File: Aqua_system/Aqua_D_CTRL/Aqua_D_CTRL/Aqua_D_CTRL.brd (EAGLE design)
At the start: 150 x 120 mm, 233 parts, among them IC1 SN65HVD3082EDR, IC2 CSTNE8M00G520000R0, IC3 LT6106CS5#TRPBF, IC4 LT6106CS5#TRPBF, IC5 TPS54202DDCR, IC6 LD1117S33TR, IC8 LM317AEMP, J1 ESP32-PICO-KIT, K1 KB20C06A, K2 KB20C06A, Q1 DMP6185SEQ-13, Q10 BC817, Q11 2N7002, Q12 DMP6185SEQ-13, Q13 2N7002, Q14 DMP6185SEQ-13, Q15 2N7002, Q16 DMP6185SEQ-13, Q17 BC817, Q18 BC817, Q19 BC817, Q2 2N7002, Q20 BC817, Q21 BC817, Q22 BC817, Q23 BC817, Q3 DMP6185SEQ-13, Q4 2N7002, Q5 DMP6185SEQ-13, Q6 DMP6185SEQ-13, Q7 2N7002, Q8 DMP6185SEQ-13, Q9 2N7002, SW1 L101011MS02Q, U1 S7G2LQFP176, X1 B2B-XH-AM(LF)(SN), X10 726386-2TE_726386-2, X11 282834-2, X12 RJ45-8L-B, X13 MICROMATCH-16, X14 RJ45-8L-B, X2 WF2549-2WS05S0B01, X3 282834-3, X4 282834-3, X5 726386-2TE_726386-2, X6 726386-2TE_726386-2, X7 726386-2TE_726386-2, X8 726386-2TE_726386-2, X9 726386-2TE_726386-2

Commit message: HW00.00 update
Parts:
- added C40: 1uF/25V, Labops_Lib_AH:0603
- added C41: 100nF/50V, Labops_Lib_AH:0603
- added R84: 10K 1%, Labops_Lib_AH:R0603
- moved C59 7.49 mm to (71.5, 49.1)
- moved C44 3.81 mm to (81.0, 72.1)
- moved C55 3.81 mm to (83.1, 72.1)
- moved C56 2.79 mm to (71.4, 55.9)
- moved X2 2.54 mm to (64.9, 73.3)
- moved C57 0.89 mm to (71.4, 53.7)
- moved D9 0.18 mm to (63.9, 23.7), turned to 180 degrees
- moved D5 0.13 mm to (67.3, 23.7), turned to 180 degrees
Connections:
- removed net MCU_RESET: U1.67
- removed net N$87: C58.2, U1.97
- new net NRST: C41.1, R84.2, U1.67, X2.10
- net GND: now also C40.2, C41.2, X2.3, X2.5, X2.9
- net VCC: now also C40.1, C58.2, R84.1, U1.97, X2.1
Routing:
- net VCC: track 320.1 -> 391.5 mm, vias 6 -> 16
- net DO_PH_SENSOR_ON: track 0.00 -> 38.0 mm, vias 0 -> 2
- net NRST: track 0.00 -> 34.2 mm, vias 0 -> 1
- net GND: track 35.5 -> 44.4 mm
- net AI_I_SENSE_PH_SENSOR: track 41.3 -> 36.3 mm
- net N$87: track 3.91 -> 0.00 mm
- net DBG_SWO: track 14.3 -> 16.7 mm
- net DBG_SWCLK: track 13.0 -> 15.1 mm
- net AI_I_SENSE_CONDUTIV_SENSOR: track 25.1 -> 26.4 mm
- net DBG_SWDIO: track 12.4 -> 13.5 mm

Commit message: HW00.00 Layout Ongoing
Ongoing Changes On Layout
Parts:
- removed C54: 100nF/50V, Labops_Lib_AH:0603
- removed R98, R99: 10K 1%, Labops_Lib_AH:R0603
- removed U1: S7G2LQFP176, 3D_MIG_Controller:LQFP176_24X24
- added U2: RENESAS_R7FA6M5BG3CFBLQFP_144_20X20_REN-M, 3D_MIG_Controller:LQFP_144_20X20_REN-M
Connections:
- removed net N$40: U1.29
- removed net N$58: IC2.1, R93.2, U1.24
- removed net N$60: U1.30
- removed net N$72: C54.2, U1.62
- removed net N$85: R98.2, U1.64
- removed net N$86: R99.2, U1.65
- removed net N$93: U1.160
- new net AVCC0: U2.127
- new net AVSS0: U2.128
- new net N$66: IC2.1, R93.2, U2.20
- new net VBATT: U2.14
- new net VCC_2: U2.81
- new net VCC_3: U2.90
- new net VCC_4: U2.99
- new net VCC_5: U2.111
- new net VCC_6: U2.121
- new net VCC_USBHS: U2.40
- new net VCL: U2.92
- new net VREFH: U2.126
- new net VREFH0: U2.130
- new net VREFL: U2.125
- new net VREFL0: U2.129
- new net VSS: U2.141
- new net VSS_2: U2.82
- new net VSS_3: U2.91
- new net VSS_4: U2.100
- new net VSS_5: U2.112
- new net VSS_6: U2.122
- new net VSS_USB: U2.37
- net /DO_COMM_RX_EN: now also U2.32; no longer U1.40
- net AI_24V0: no longer U1.144
- net AI_I_SENSE_CONDUTIV_SENSOR: no longer U1.146
- net AI_I_SENSE_PH_SENSOR: no longer U1.140
- net AI_V_PH_SENSOR: no longer U1.142
- net DBG_SWCLK: now also U2.72; no longer U1.88
- net DBG_SWDIO: now also U2.73; no longer U1.89
- net DBG_SWO: now also U2.74; no longer U1.90
- net DI_DOSING_EN: now also U2.31; no longer U1.39
- net DI_UART_RX_ESP32: now also U2.71; no longer U1.87
- net DI_USART_RX: now also U2.35; no longer U1.43
- net DO_7XSEGMENT_1_EN: now also U2.1; no longer U1.1
- net DO_7XSEGMENT_2_EN: now also U2.2; no longer U1.2
- net DO_7XSEGMENT_3_EN: now also U2.3; no longer U1.3
- net DO_BCD_A: no longer U1.130
- net DO_BCD_B: no longer U1.129
- net DO_BCD_C: no longer U1.128
- net DO_BCD_D: no longer U1.127
- net DO_COMM_TX_EN: now also U2.33; no longer U1.41
- net DO_CONDUCTIV_PUMP_ON_LED: now also U2.8; no longer U1.8
- net DO_CONDUCTIV_SENSOR_DISPLAY_ON: now also U2.7; no longer U1.7
- net DO_CONDUCTIV_SENSOR_ON: no longer U1.132
- net DO_CTRL_GREEN_STATUS_LED: now also U2.5; no longer U1.5
- net DO_CTRL_RED_STATUS_LED: now also U2.6; no longer U1.6
- net DO_CTRL_YELLOW_STATUS_LED: now also U2.4; no longer U1.4
- net DO_ESP32_EN: now also U2.69; no longer U1.85
- net DO_PH_PUMP_ON_LED: now also U2.10; no longer U1.10
- net DO_PH_SENSOR_DISPLAY_ON: now also U2.9; no longer U1.9
- net DO_PH_SENSOR_ON: no longer U1.131
- net DO_UART_TX_ESP32: now also U2.70; no longer U1.86
- net DO_USART_TX: now also U2.34; no longer U1.42
- net DO_V_CONDUCTIV_PUMP_ON: no longer U1.91
- net DO_V_PH_PUMP_ON: no longer U1.92
- net GND: now also U2.18, U2.48, U2.67; no longer C54.1, R98.1, R99.1, U1.111, U1.124, U1.139, U1.150, U1.156, U1.157, U1.170, U1.22, U1.28, U1.35, U1.45, U1.60, U1.63, U1.66, U1.83, U1.98
- net N$55: now also U2.19; no longer U1.23
- net N$59: no longer U1.27
- net N$63: now also U2.15; no longer U1.19
- net N$88: no longer U1.112
- net N$90: no longer U1.148
- net NRST: now also U2.55; no longer U1.67
- net VCC: now also U2.142, U2.21, U2.49, U2.68; no longer U1.110, U1.123, U1.138, U1.149, U1.155, U1.158, U1.171, U1.25, U1.61, U1.84, U1.97
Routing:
- net VCC: track 391.5 -> 368.8 mm
- net DO_7XSEGMENT_1_EN: track 19.8 -> 2.12 mm
- net DO_V_CONDUCTIV_PUMP_ON: track 32.1 -> 20.9 mm
- net DO_V_PH_PUMP_ON: track 14.1 -> 3.30 mm
- net N$58: track 8.07 -> 0.00 mm
- net DBG_SWCLK: track 15.1 -> 9.12 mm
- net DO_COMM_TX_EN: track 5.33 -> 0.21 mm
- net N$72: track 4.86 -> 0.00 mm
- net N$66: track 0.00 -> 4.65 mm
- net N$85: track 4.43 -> 0.00 mm
- net N$86: track 4.21 -> 0.00 mm
- net DBG_SWO: track 16.7 -> 12.5 mm
- net DO_UART_TX_ESP32: track 4.04 -> 0.14 mm
- net DO_USART_TX: track 5.97 -> 2.38 mm
- net DBG_SWDIO: track 13.5 -> 10.4 mm
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
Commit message: HW00.00 ongoing
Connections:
- removed net VCC_2: U2.81
- removed net VCC_3: U2.90
- removed net VCC_4: U2.99
- removed net VCL: U2.92
- removed net VSS_2: U2.82
- removed net VSS_3: U2.91
- removed net VSS_4: U2.100
- net DO_BCD_A: now also U2.106
- net DO_BCD_B: now also U2.105
- net DO_BCD_C: now also U2.104
- net DO_BCD_D: now also U2.103
- net DO_CONDUCTIV_SENSOR_ON: now also U2.108
- net DO_PH_SENSOR_ON: now also U2.107
- net DO_V_CONDUCTIV_PUMP_ON: now also U2.75
- net DO_V_PH_PUMP_ON: now also U2.76
- net GND: now also U2.100, U2.82, U2.91
- net N$88: now also U2.92
- net VCC: now also U2.81, U2.90, U2.99
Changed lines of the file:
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@@
 <contactref element="U2" pad="48"/>
 <contactref element="U2" pad="67"/>
+<contactref element="U2" pad="82"/>
+<contactref element="U2" pad="91"/>
+<contactref element="U2" pad="100"/>
 <wire x1="130.214" y1="99.822" x2="131.358" y2="117.094" width="0" layer="19" extent="1-1"/>
 <wire x1="125.818" y1="99.822" x2="128.866" y2="99.822" width="0" layer="19" extent="1-1"/>
@@
 <wire x1="48.094" y1="80.01" x2="50.275" y2="77.216" width="0" layer="19" extent="1-1"/>
 <wire x1="80.518" y1="64.69575" x2="81.026" y2="72.986" width="0" layer="19" extent="1-1"/>
+<wire x1="76.02025" y1="58.166" x2="80.518" y2="64.69575" width="0" layer="19" extent="1-1"/>
+<wire x1="76.02025" y1="53.594" x2="76.02025" y2="58.166" width="0" layer="19" extent="1-1"/>
+<wire x1="76.02025" y1="49.022" x2="76.02025" y2="53.594" width="0" layer="19" extent="1-1"/>
+<wire x1="70.651" y1="49.149" x2="76.02025" y2="49.022" width="0" layer="19" extent="1-1"/>
+<wire x1="70.524" y1="60.96" x2="70.524" y2="55.88" width="0" layer="19" extent="1-1"/>
 <wire x1="90.17" y1="64.69575" x2="86.995" y2="72.986" width="0" layer="19" extent="1-1"/>
+<wire x1="72.048" y1="40.386" x2="70.651" y2="49.149" width="0" layer="19" extent="1-1"/>
 <wire x1="70.612" y1="92.749" x2="79.604" y2="96.266" width="0" layer="19" extent="1-1"/>
 <wire x1="68.58" y1="92.749" x2="70.612" y2="92.749" width="0" layer="19" extent="1-1"/>
 <wire x1="62.738" y1="94.742" x2="68.58" y2="92.749" width="0" layer="19" extent="1-1"/>
 <wire x1="60.198" y1="90.082" x2="62.738" y2="94.742" width="0" layer="19" extent="1-1"/>
-<wire x1="70.524" y1="60.96" x2="60.198" y2="62.904" width="0" layer="19" extent="1-1"/>
-<wire x1="70.524" y1="55.88" x2="70.524" y2="60.96" width="0" layer="19" extent="1-1"/>
-<wire x1="72.048" y1="40.386" x2="70.651" y2="49.149" width="0" layer="19" extent="1-1"/>
 <wire x1="59.563" y1="44.87" x2="70.651" y2="49.149" width="0" layer="19" extent="1-1"/>
 <wire x1="55.819" y1="46.566" x2="59.563" y2="44.87" width="0" layer="19" extent="1-1"/>
@@
 <contactref element="U2" pad="21"/>
 <contactref element="U2" pad="49"/>
+<contactref element="U2" pad="81"/>
+<contactref element="U2" pad="90"/>
+<contactref element="U2" pad="99"/>
 <wire x1="115.316" y1="74.002" x2="113.284" y2="74.002" width="0" layer="19" extent="1-1"/>
 <wire x1="97.71575" y1="55.118" x2="102.088" y2="55.86" width="0" layer="19" extent="1-1"/>
@@
 <wire x1="84.836" y1="69.596" x2="91.396" y2="69.044" width="0" layer="19" extent="1-1"/>
 <wire x1="95.758" y1="38.442" x2="95.758" y2="38.481" width="0" layer="19" extent="1-1"/>
+<wire x1="76.02025" y1="54.102" x2="73.244" y2="54.86" width="0" layer="19" extent="1-1"/>
+<wire x1="76.02025" y1="49.53" x2="73.14" y2="48.36" width="0" layer="19" extent="1-1"/>
+<wire x1="76.02025" y1="58.674" x2="74.187" y2="61.36" width="0" layer="19" extent="1-1"/>
 <wire x1="80.01" y1="64.69575" x2="79.896" y2="68.847" width="0" layer="19" extent="1-1"/>
 <wire x1="66.36" y1="24.749" x2="66.548" y2="28.956" width="0" layer="19" extent="1-1"/>
@@
 <wire x1="64.174" y1="62.904" x2="62.23" y2="62.904" width="0.254" layer="1"/>
 <wire x1="65.13" y1="63.86" x2="64.174" y2="62.904" width="0.254" layer="1"/>
+<contactref element="U2" pad="76"/>
+<wire x1="65.13" y1="63.86" x2="76.02025" y2="61.214" width="0" layer="19" extent="1-1"/>
 </signal>
 <signal name="V_PH" class="3">
@@
 <wire x1="77.089" y1="42.164" x2="77.089" y2="44.069" width="0.2032" layer="1"/>
 <wire x1="77.089" y1="44.069" x2="76.798" y2="44.36" width="0.2032" layer="1"/>
+<contactref element="U2" pad="107"/>
+<wire x1="76.798" y1="44.36" x2="76.02025" y2="45.466" width="0" layer="19" extent="1-1"/>
 </signal>
 <signal name="AI_I_SENSE_PH_SENSOR" class="3">
@@
 <wire x1="64.389" y1="47.664" x2="61.595" y2="44.87" width="0.254" layer="1"/>
 <wire x1="64.389" y1="61.976" x2="64.389" y2="47.664" width="0.254" layer="1"/>
+<contactref element="U2" pad="75"/>
+<wire x1="64.741" y1="64.36" x2="76.02025" y2="61.722" width="0" layer="19" extent="1-1"/>
 </signal>
 <signal name="V_CONDUCTIV" class="3">
@@
 <signal name="DO_CONDUCTIV_SENSOR_ON" class="3">
 <contactref element="R27" pad="2"/>
+<contactref element="U2" pad="108"/>
+<wire x1="75.946" y1="24.472" x2="76.02025" y2="44.958" width="0" layer="19" extent="1-1"/>
 </signal>
 <signal name="CONDUCTIV_PUMP_MAINS_L_SW" class="4">
@@
 <via x="78.232" y="44.958" extent="1-16" drill="0.35"/>
 <wire x1="78.232" y1="44.958" x2="78.134" y2="44.86" width="0.254" layer="1"/>
+<contactref element="U2" pad="106"/>
 <wire x1="141.39" y1="16.256" x2="143.09" y2="16.256" width="0" layer="19" extent="1-1"/>
+<wire x1="76.02025" y1="45.974" x2="78.134" y2="44.86" width="0" layer="19" extent="1-1"/>
 </signal>
 <signal name="DO_BCD_C" class="3">
@@
 <wire x1="80.772" y1="46.482" x2="78.0382625" y2="46.482" width="0.254" layer="1"/>
 <wire x1="78.0382625" y1="46.482" x2="77.4162625" y2="45.86" width="0.254" layer="1"/>
+<contactref element="U2" pad="104"/>
 <wire x1="141.39" y1="12.192" x2="143.09" y2="12.192" width="0" layer="19" extent="1-1"/>
+<wire x1="76.02025" y1="46.99" x2="77.4162625" y2="45.86" width="0" layer="19" extent="1-1"/>
 </signal>
 <signal name="DBG_SWCLK" class="3">
@@
 <wire x1="141.39" y1="18.288" x2="137.922" y2="18.288" width="0.254" layer="1"/>
 <wire x1="77.978" y1="45.72" x2="77.618" y2="45.36" width="0.254" layer="1"/>
+<contactref element="U2" pad="105"/>
+<wire x1="76.02025" y1="46.482" x2="77.618" y2="45.36" width="0" layer="19" extent="1-1"/>
 </signal>
 <signal name="N$43" class="3">
@@
 <wire x1="79.4004" y1="47.0154" x2="77.869925" y2="47.0154" width="0.254" layer="1"/>
 <wire x1="77.869925" y1="47.0154" x2="77.214525" y2="46.36" width="0.254" layer="1"/>
+<contactref element="U2" pad="103"/>
+<wire x1="76.02025" y1="47.498" x2="77.214525" y2="46.36" width="0" layer="19" extent="1-1"/>
 </signal>
 <signal name="N$5">
@@
 <wire x1="72.224" y1="53.721" x2="72.351" y2="53.848" width="0.254" layer="1"/>
 <wire x1="72.351" y1="53.848" x2="75.9594" y2="53.848" width="0.254" layer="1"/>
+<contactref element="U2" pad="92"/>
+<wire x1="76.02025" y1="53.086" x2="75.9594" y2="53.848" width="0" layer="19" extent="1-1"/>
 </signal>
 <signal name="N$90" class="3">
@@
 <contactref element="U2" pad="14"/>
 </signal>
-<signal name="VSS_2">
-<contactref element="U2" pad="82"/>
-</signal>
-<signal name="VCC_2">
-<contactref element="U2" pad="81"/>
-</signal>
 <signal name="VSS_USB">
 <contactref element="U2" pad="37"/>
@@
 <contactref element="U2" pad="40"/>
 </signal>
-<signal name="VSS_3">
-<contactref element="U2" pad="91"/>
-</signal>
-<signal name="VCC_3">
-<contactref element="U2" pad="90"/>
-</signal>
 <signal name="VSS">
 <contactref element="U2" pad="141"/>
 </signal>
-<signal name="VCL">
-<contactref element="U2" pad="92"/>
-</signal>
-<signal name="VCC_4">
-<contactref element="U2" pad="99"/>
-</signal>
-<signal name="VSS_4">
-<contactref element="U2" pad="100"/>
-</signal>
 <signal name="VCC_5">

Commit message: HW00.00 Ongoing
Layout ongoing
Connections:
- removed net AVCC0: U2.127
- removed net AVSS0: U2.128
- removed net N$90: C67.2
- removed net VCC_5: U2.111
- removed net VCC_6: U2.121
- removed net VREFH0: U2.130
- removed net VREFL0: U2.129
- removed net VSS: U2.141
- removed net VSS_5: U2.112
- removed net VSS_6: U2.122
- net AI_24V0: now also U2.115
- net AI_I_SENSE_CONDUTIV_SENSOR: now also U2.116
- net AI_I_SENSE_PH_SENSOR: now also U2.113
- net AI_V_CONDUCTIV_SENSOR: now also U2.117
- net AI_V_PH_SENSOR: now also U2.114
- net GND: now also U2.112, U2.122, U2.128, U2.129, U2.141
- net VCC: now also C67.2, U2.111, U2.121, U2.127, U2.130
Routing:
- net N$90: track 2.84 -> 0.00 mm

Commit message: HW00.00 Layout Ongoing
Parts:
- removed R95: 2.2K 1%, Labops_Lib_AH:R0603
- C67: value 100nF/50V -> 1unF/50V
- U2: value RENESAS_R7FA6M5BG3CFBLQFP_144_20X20_REN-M -> R7FA6M5BG3CFBLQFP_144_20X20_REN-M; device 3D_MIG_Controller:LQFP_144_20X20_REN-M -> Labops_Lib_AH:LQFP_144_20X20_REN-M
- moved C67 14.4 mm to (97.9, 37.6)
- moved D13 6.23 mm to (116.0, 59.6), turned to 180 degrees
- moved C53 5.97 mm to (89.0, 72.1)
- moved C58 3.05 mm to (71.4, 57.9)
- moved IC2 3.02 mm to (105.5, 55.0), turned to 0 degrees
- moved R93 3.01 mm to (102.5, 54.2), turned to 90 degrees
- moved C60 1.91 mm to (95.9, 37.6)
- moved C61 1.91 mm to (91.8, 37.6)
- moved C62 1.91 mm to (93.9, 37.6)
- moved C63 1.91 mm to (89.8, 37.6)
- moved C64 1.91 mm to (87.8, 37.6)
- moved C65 1.91 mm to (85.7, 37.6)
- moved C68 1.91 mm to (83.7, 37.6)
- moved C57 1.78 mm to (71.5, 51.9)
- moved U2 1.17 mm to (86.6, 52.7)
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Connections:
- removed net N$59: R95.2
- removed net VREFH: U2.126
- removed net VREFL: U2.125
- new net VREFH0: U2.130
- new net VREFL0: U2.129
- net GND: now also U2.125; no longer R95.1, U2.129
- net VCC: now also U2.126; no longer U2.130
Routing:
- net DO_7XSEGMENT_1_EN: track 2.12 -> 22.6 mm
- net AI_V_CONDUCTIV_SENSOR: track 15.8 -> 36.0 mm, vias 0 -> 2
- net DO_V_PH_PUMP_ON: track 3.30 -> 14.7 mm
- net DO_COMM_TX_EN: track 0.21 -> 11.0 mm
- net GND: track 44.4 -> 55.1 mm, vias 1 -> 0
- net DO_V_CONDUCTIV_PUMP_ON: track 20.9 -> 30.5 mm
- net V_5V0: track 129.4 -> 138.7 mm
- net DO_USART_TX: track 2.38 -> 11.4 mm
- net DO_UART_TX_ESP32: track 0.14 -> 7.98 mm
- net N$1: track 16.4 -> 24.1 mm
- net DBG_SWCLK: track 9.12 -> 16.5 mm
- net DI_USART_RX: track 14.2 -> 21.1 mm
- net /DO_COMM_RX_EN: track 3.39 -> 10.1 mm
- net DBG_SWO: track 12.5 -> 19.2 mm
- net DO_PH_PUMP_ON_LED: track 24.4 -> 31.0 mm
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
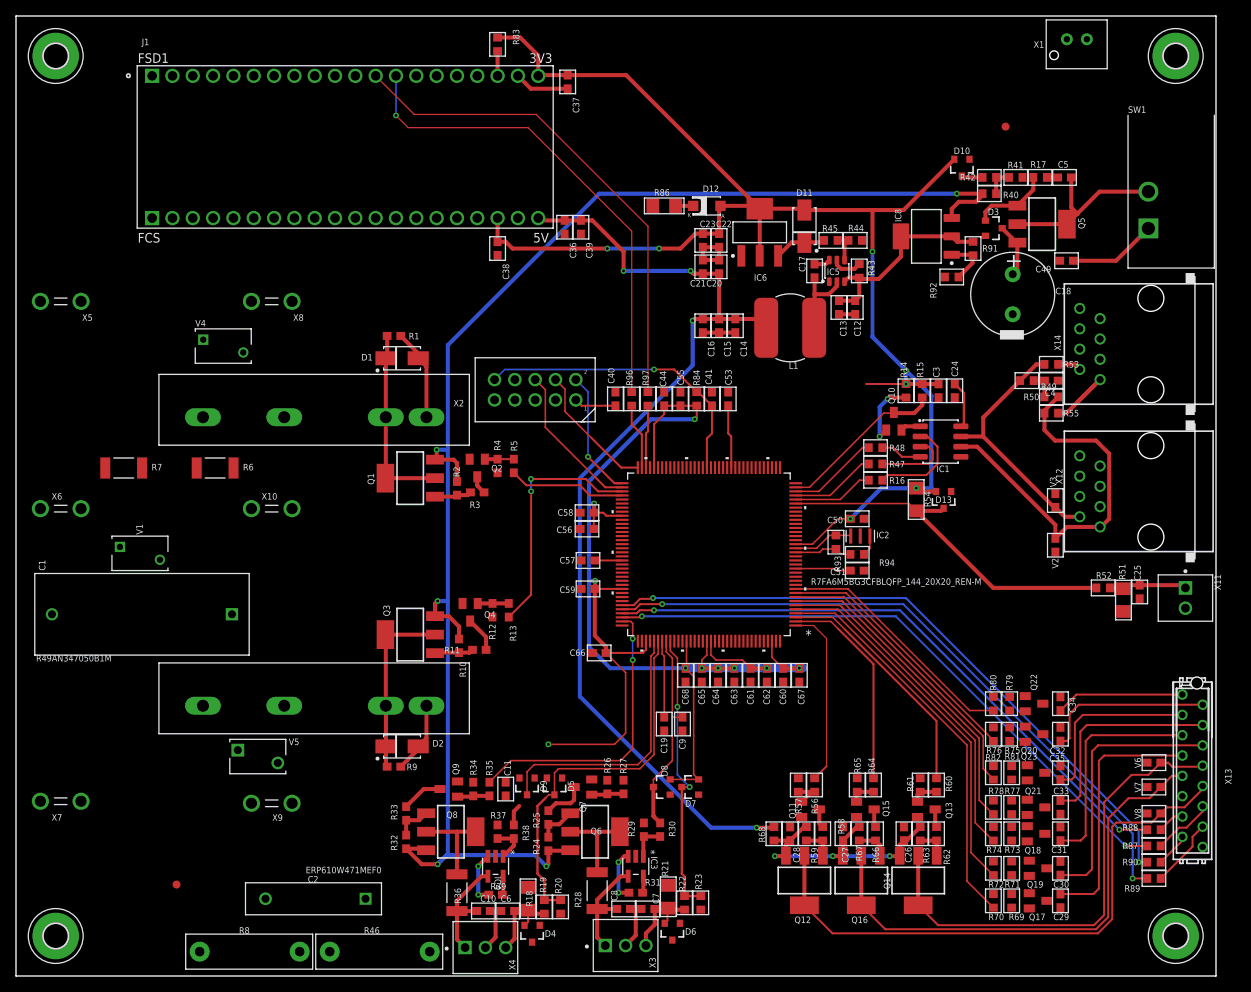
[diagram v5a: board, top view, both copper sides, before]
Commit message: HW00.00 Ongoing
Layout Copper Pouring
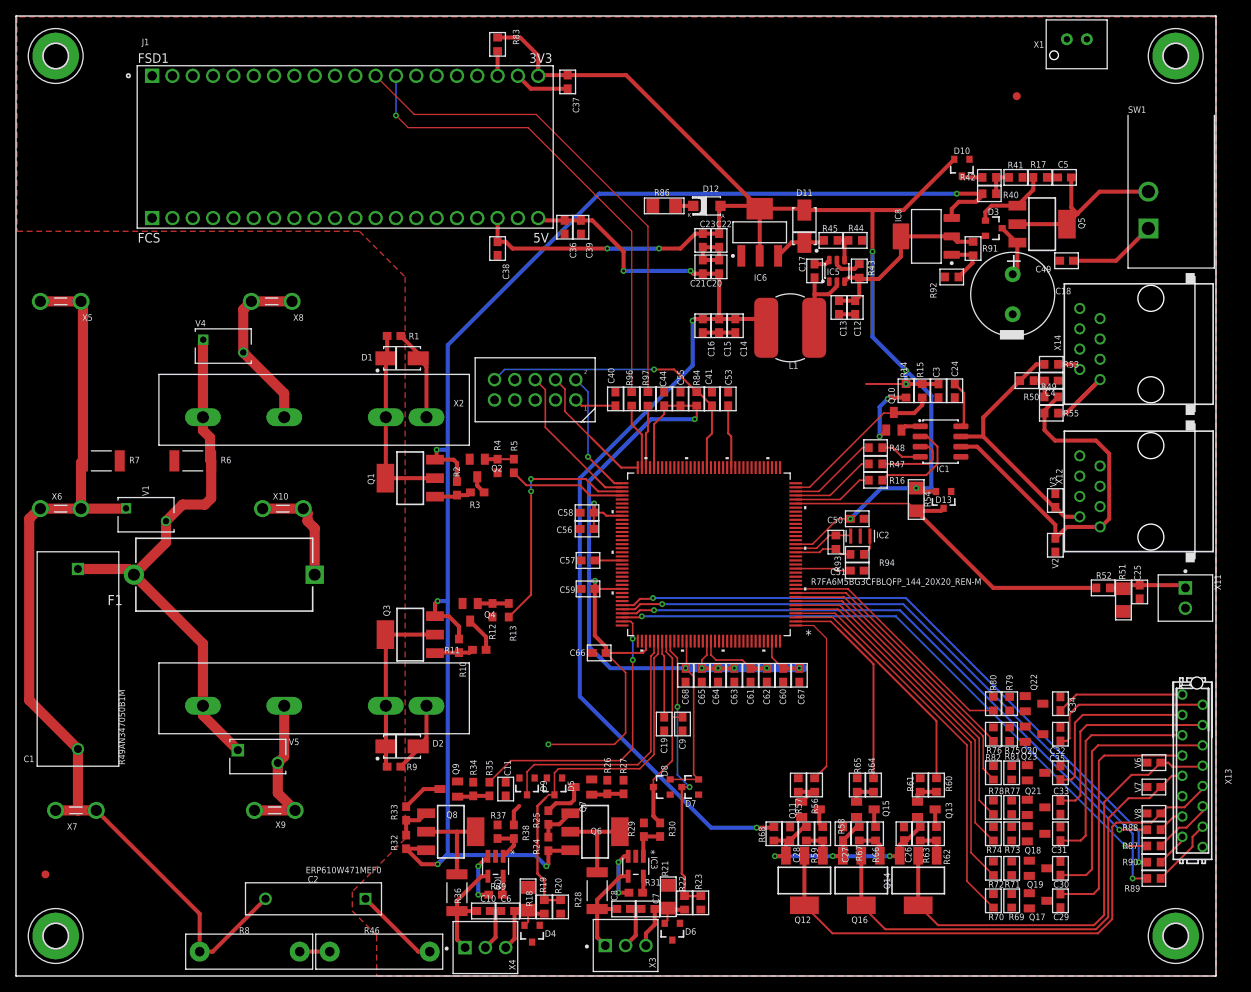
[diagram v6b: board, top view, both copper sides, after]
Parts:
- added F1: 696101000002, Labops_Lib_AH:FUSE_RM22.6
- moved FID1 16.4 mm to (3.68, 12.7)
- moved C1 9.76 mm to (7.75, 39.6), turned to 270 degrees
- moved V1 4.89 mm to (16.3, 57.7)
- moved FID2 4.06 mm to (125.1, 110.0)
- moved R6 2.93 mm to (22.1, 64.4)
- moved R7 2.93 mm to (10.7, 64.4)
- moved X7 2.22 mm to (7.49, 20.7)
- moved X10 1.40 mm to (33.4, 58.4)
- moved X9 0.97 mm to (32.3, 20.7)
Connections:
- new net MAINS_L_F: C1.1, F1.2, K1.P$4, K2.P$4, R6.2, V1.2, V4.1, V5.1
- net MAINS_L: now also F1.1; no longer C1.1, K1.P$4, K2.P$4, R6.2, V1.2, V4.1, V5.1
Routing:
- net MAINS_N: track 0.00 -> 121.9 mm
- net MAINS_L_F: track 0.00 -> 70.1 mm
- net PH_PUMP_MAINS_L_SW: track 0.00 -> 22.1 mm
- net CONDUCTIV_PUMP_MAINS_L_SW: track 0.00 -> 19.4 mm
- net MAINS_L: track 0.00 -> 13.9 mm
- net GND: track 55.1 -> 65.9 mm
- net N$28: track 0.00 -> 3.76 mm
- added copper zone on layer 1, net GND...

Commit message: HW00.00 Layout ongoing
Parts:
- moved R73 0.13 mm to (124.5, 17.7)
- moved R74 0.13 mm to (122.2, 17.7)
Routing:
- net N$71: track 0.00 -> 6.18 mm
- net N$65: track 0.00 -> 6.03 mm
- net N$62: track 0.00 -> 5.81 mm
- net N$68: track 0.00 -> 5.58 mm
- net N$45: track 0.00 -> 5.22 mm
- net N$51: track 0.00 -> 5.13 mm
- net N$57: track 0.00 -> 4.79 mm
- net GND: track 65.9 -> 69.9 mm, vias 0 -> 2
- net /PH_PUMP_LED_ON: track 16.1 -> 18.6 mm
- net /PH_SENSOR_LED_ON: track 21.4 -> 24.0 mm
- net /STATUS_LED_R: track 27.6 -> 29.9 mm
- net /CONDUCTIV_SENSOR_LED_ON: track 26.4 -> 28.7 mm
- net /CONDUCTIV_PUMP_LED_ON: track 22.5 -> 24.8 mm
- net N$50: track 0.00 -> 2.24 mm
- net N$44: track 0.00 -> 2.24 mm
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- added copper zone on layer 1, net GND
- added copper zone on layer 16, net GND
- removed copper zone on layer 1, net GND...
